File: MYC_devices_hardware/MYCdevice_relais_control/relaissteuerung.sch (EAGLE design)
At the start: 54 parts, among them IC1 MEGA8-P, IC2 7805T, K1 RT424012, K2 RT424012, K3 RT424012, K4 RT424012, Q1 20MHz, T1 BC547, T2 BC547, T3 BC547, T4 BC547

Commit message: adation to "0" based, and minor changes
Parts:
- removed C8: 18pF, resistor:C-EU050-025X075
- removed C9: 100nF, resistor:C-EU050-025X075
- removed R10: 3.3k, eagle-ltspice:R0204/7
- added JP2: ISP, jumper:JP3Q
- added R12: 3.3k, rcl:R-EU_0204/2V
- added X4, X5: 1503_09, con-lumberg:1503_09
- C1: value 100nF -> 22u 1206; device resistor:C-EU050-025X075 -> resistor:C-EUC1206
- C2, C3: value 47uF -> 22u 1206; device rcl:CPOL-EUTT5D10 -> resistor:C-EUC1206
- C4: value 100nF -> 18pF
- C6: device resistor:C-EU050-025X075 -> resistor:C-EUC1206
- D1, D2, D3, D4, D5: device diode:1N4004 -> zetex:D_E2L
- IC2: value 7805T -> 7805TV; device linear:7805T -> linear:7805TV
- R1, R2, R4, R6: device rcl:R-EU_0204/7 -> rcl:R-EU_0204/2V
- R8: device eagle-ltspice:R0204/7 -> rcl:R-EU_0204/2V
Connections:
- net N$37 renamed C5
- removed net N$1: IC1.PC4(ADC4/SDA), R2.2, SL1.5
- new net N$37: IC1.PC4(ADC4/SDA), R2.2, SL1.5, X4.3, X5.3
- new net N$56: C16.2, IC1.PB5(SCK), JP2.3, X1.-5
- net GND: now also C2.2, C3.1, C4.1, JP2.6, X4.1, X5.1; no longer C2.-, C3.-, C4.2, C8.1, C9.1
- net N$13: now also R8.2; no longer R6.1
- net N$15: now also R12.1; no longer R4.1
- net N$19: now also C4.2; no longer C8.2
- net N$22: now also R8.1; no longer R6.2
- net N$23: now also JP2.4
- net N$26: now also R6.1; no longer R8.1
- net N$3: no longer C2.+
- net N$33: now also JP2.1
- net N$34: now also R6.2; no longer R8.2
- net N$35: now also C3.2; no longer C9.2
- net N$36: now also R12.2; no longer R4.2
- net N$5: now also X4.2, X5.2
- net N$67: now also R4.2; no longer R10.2
- net N$69: now also R4.1; no longer R10.1
- net N$7: now also IC1.PC6(/RESET), JP2.5; no longer C16.2, IC1.PB5(SCK), X1.-5
- net VDD: now also C2.1, JP2.2; no longer C3.+, C4.1
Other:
- moved on the sheet: C1, C4, R4, R6, R8, SL1

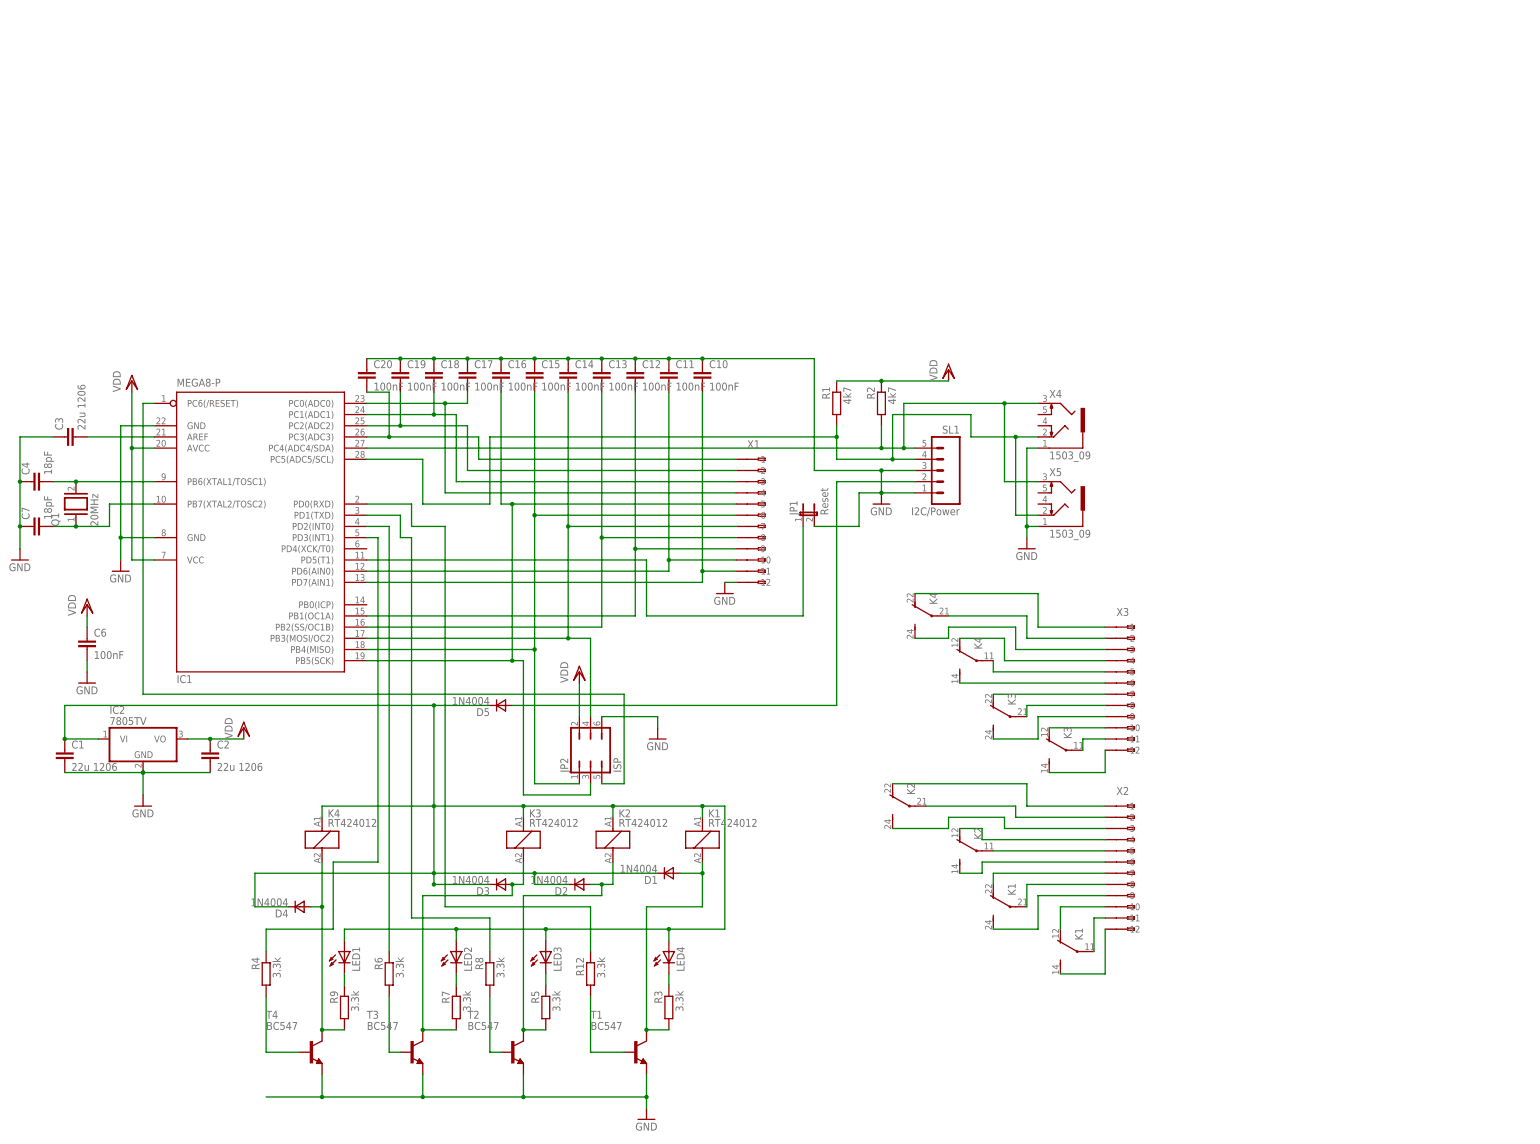
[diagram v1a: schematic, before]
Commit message: Modified Answer format
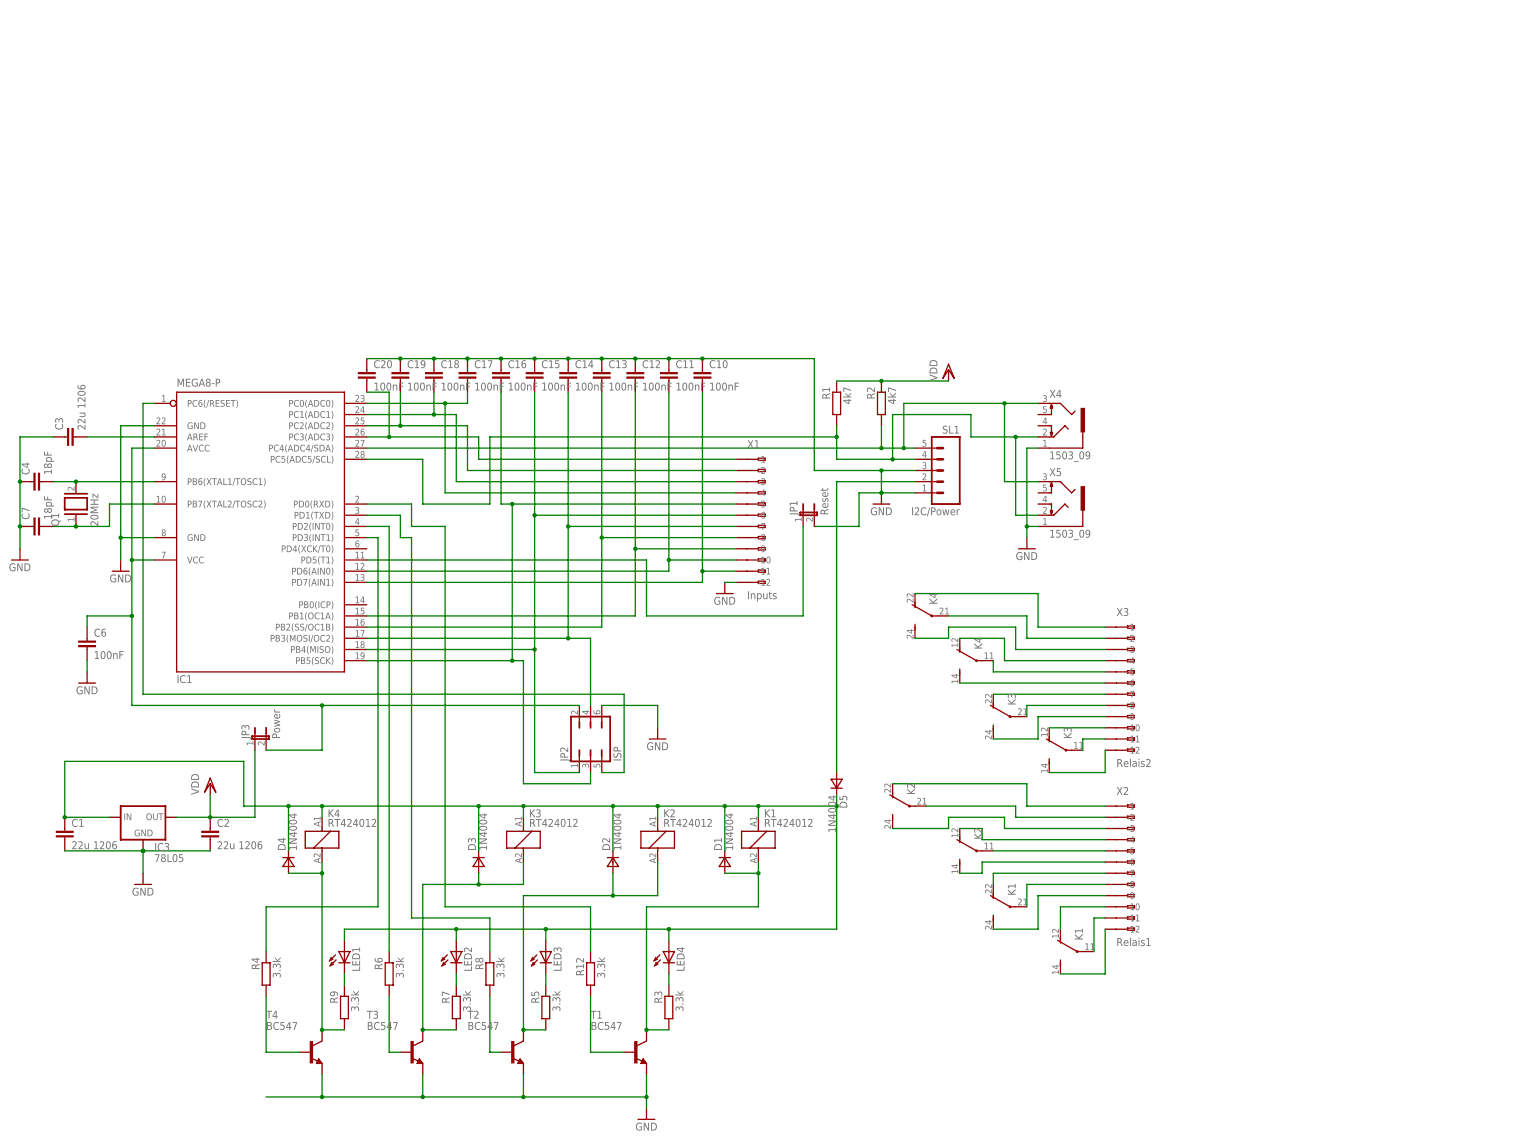
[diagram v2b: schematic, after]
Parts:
- removed IC2: 7805TV, linear:7805TV
- added IC3: 78L05, v-reg:78LXX
- added JP3: Power, jumper:JP1E
- R1, R2: device rcl:R-EU_0204/2V -> resistor:R-EU_R1206
- X1: value (none) -> Inputs
- X2: value (none) -> Relais1
- X3: value (none) -> Relais2
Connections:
- new net N$58: C6.1, IC1.AVCC, IC1.VCC@1, JP2.2, JP3.2
- net GND: now also IC3.GND; no longer IC2.GND
- net N$3: now also IC3.IN; no longer IC2.VI
- net VDD: now also IC3.OUT, JP3.1; no longer C6.1, IC1.AVCC, IC1.VCC@1, IC2.VO, JP2.2
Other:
- moved on the sheet: C1, C2, D1, D2, D3, D4, D5, JP2, K1, K2

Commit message: new connector, I2C with 3V
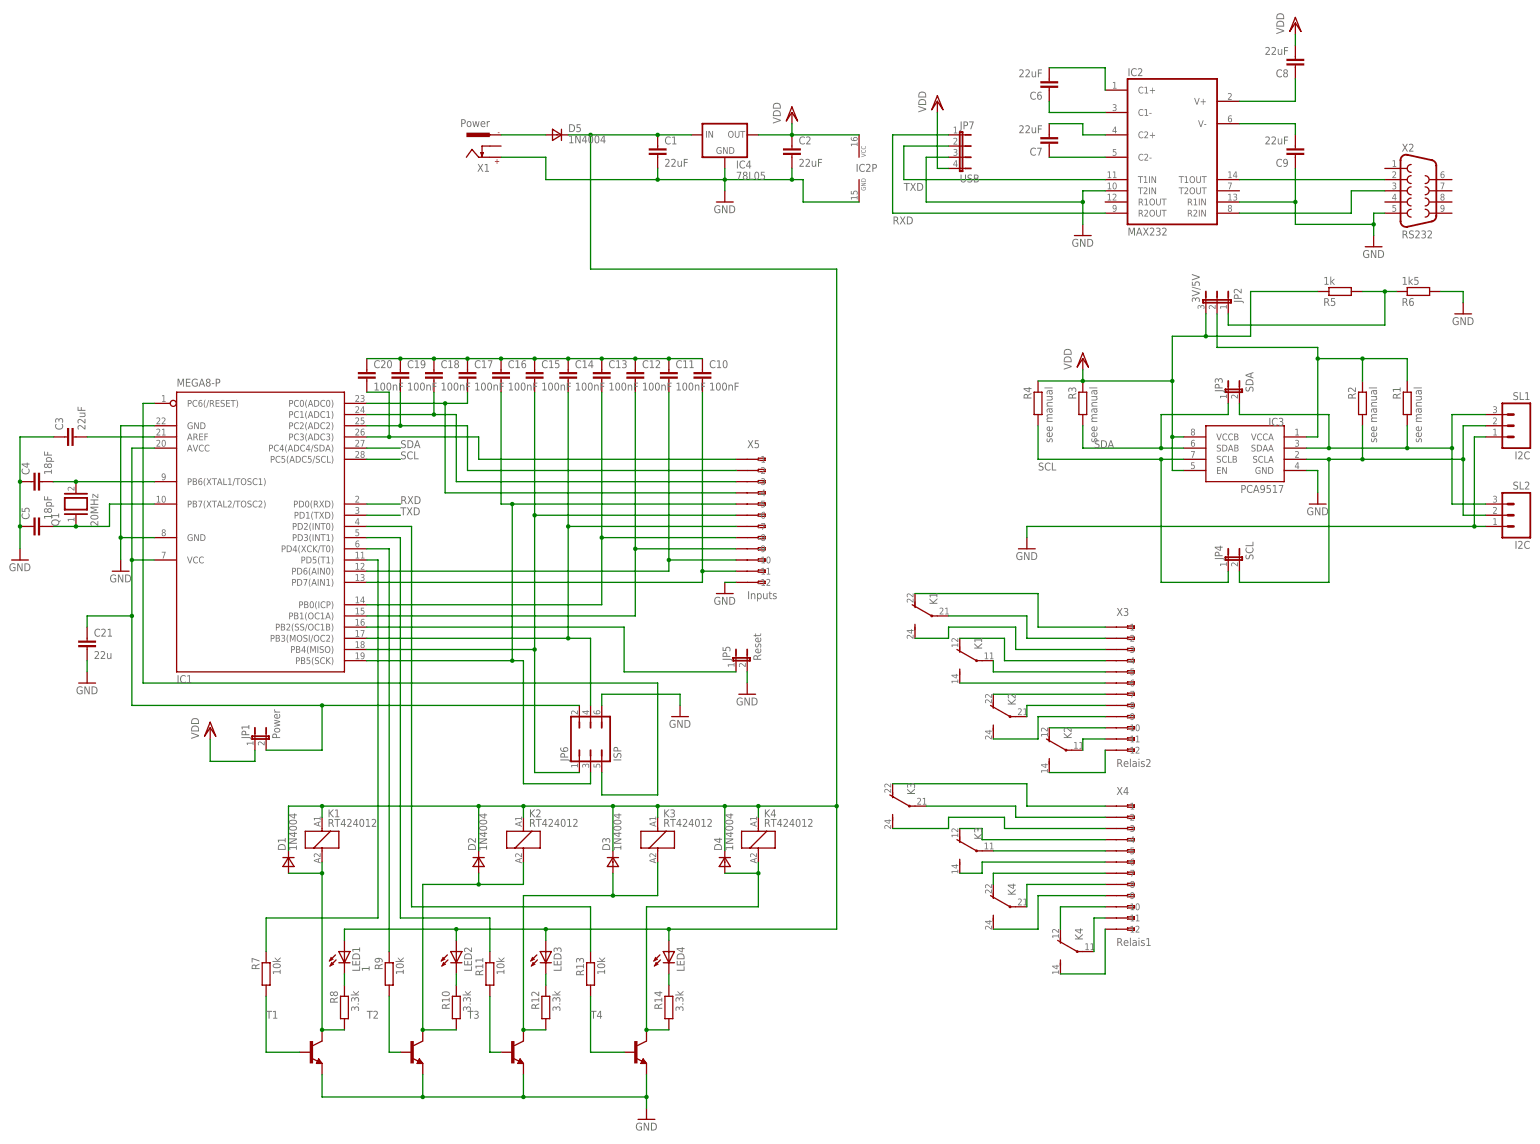
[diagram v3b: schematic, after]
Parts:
- added C21: 22u, resistor:C-EUC1206
- added C5: 18pF, resistor:C-EU050-025X075
- added C8, C9: 22uF, rcl:C-EUC1206
- added IC2: MAX232, maxim:MAX232
- added IC4: 78L05, v-reg:78LXX
- added JP4: SCL, jumper:JP1E
- added JP5: Reset, jumper:JP1E
- added JP6: ISP, jumper:JP3Q
- added JP7: USB, jumper:JP4E
- added R10, R14: 3.3k, rcl:R-EU_R1206
- added R11: 10k, rcl:R-EU_R1206
- added R13: 10k, rcl:R-EU_M1206
- added SL2: I2C, con-amp-quick:M03
- C1, C2, C3: value 22u 1206 -> 22uF
- C10, C11, C12, C13, C14, C15, C16, C17, C18, C19, C20: device resistor:C-EU050-025X075 -> resistor:C-EUC1206
- C6: value 100nF -> 22uF; device resistor:C-EUC1206 -> rcl:C-EUC1206
- C7: value 18pF -> 22uF; device resistor:C-EU050-025X075 -> rcl:C-EUC1206
- IC3: value 78L05 -> PCA9517; device v-reg:78LXX -> PCA9517:PCA9517
- JP1: value Reset -> Power
- JP2: value ISP -> 3V/5V; device jumper:JP3Q -> jumper:JP2E
- JP3: value Power -> SDA
- LED1: value (none) -> 1
- R1, R2: value 4k7 -> see manual
- R12, R8: device rcl:R-EU_0204/2V -> rcl:R-EU_R1206
- R3, R4: value 3.3k -> see manual; device rcl:R-EU_0204/2V -> resistor:R-EU_R1206
- R5: value 3.3k -> 1k; device rcl:R-EU_0204/2V -> resistor:R-EU_R1206
- R6: value 3.3k -> 1k5; device rcl:R-EU_0204/2V -> resistor:R-EU_R1206
- R7: value 3.3k -> 10k; device rcl:R-EU_0204/2V -> rcl:R-EU_R1206
- R9: value 3.3k -> 10k; device rcl:R-EU_0204/2V -> rcl:R-EU_M1206
- SL1: value I2C/Power -> I2C; device con-amp-quick:M05 -> con-amp-quick:M03
- T1, T2, T3, T4: value BC547 -> (none); device transistor:BC547 -> transistor-neu-to92:BC817-16-NPN-SOT23-BEC
- X1: value Inputs -> Power; device con-wago255:233-512 -> con-conrad:737992-55
- X2: value Relais1 -> RS232; device con-wago255:233-512 -> con-subd:F09H
- X4: value 1503_09 -> Relais1; device con-lumberg:1503_09 -> con-wago255:233-512
- X5: value 1503_09 -> Inputs; device con-lumberg:1503_09 -> con-wago255:233-512
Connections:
- new net N$57: IC3.SDAA, JP3.2, R1.2, SL1.3, SL2.3
- new net N$59: IC3.VCCA, JP2.2, R1.1, R2.1
- new net N$60: IC2G$1.T1OUT, X2.2
- new net N$63: JP2.1, R5.2, R6.1
- new net N$64: IC2G$1.R2IN, X2.3
- new net N$70: C9.2, IC2G$1.V-
- new net N$71: C8.1, IC2G$1.V+
- new net N$72: C7.1, IC2G$1.C2-
- new net N$73: C7.2, IC2G$1.C2+
- new net N$74: C6.1, IC2G$1.C1-
- new net N$75: C6.2, IC2G$1.C1+
- new net RXD: IC1.PD0(RXD), IC2G$1.R2OUT, JP7.1
- new net SCL: IC1.PC5(ADC5/SCL), IC3.SCLB, JP4.1, R4.2
- new net SDA: IC1.PC4(ADC4/SDA), IC3.SDAB, JP3.1, R3.2
- new net TXD: IC1.PD1(TXD), IC2G$1.T1IN, JP7.2
- net C5: now also C5.2; no longer C7.2
- net GND: now also C21.2, C5.1, C9.1, IC2G$1.R1IN, IC2G$1.T2IN, IC2P.GND, IC4.GND, JP5.2, JP6.6, JP7.3, R6.2, SL2.1, X1.+, X2.5, X5.-12; no longer C10.1, C11.1, C12.1, C13.1, C14.1, C15.1, C16.1, C17.1, C18.1, C19.1, C20.1, C6.2, C7.1, JP1.2, JP2.6, SL1.3, X1.-12, X4.1, X5.1
- net N$10: now also K43.S, X4.-9; no longer K13.S, X2.-9
- net N$11: now also K43.P, X4.-8; no longer K13.P, X2.-8
- net N$12: now also K43.O, X4.-7; no longer K13.O, X2.-7
- net N$13: now also R11.2, T3.B; no longer R8.2, T2.B
- net N$15: now also IC1.PD5(T1), R7.1; no longer IC1.PD0(RXD), R12.1
- net N$16: now also K32.S, X4.-6; no longer K22.S, X2.-6
- net N$17: now also K32.P, X4.-5; no longer K22.P, X2.-5
- net N$18: now also K32.O, X4.-4; no longer K22.O, X2.-4
- net N$2: now also K42.S, X4.-12; no longer K12.S, X2.-12
- net N$20: now also X5.-3; no longer X1.-3
- net N$21: now also IC1.PB2(SS/OC1B), JP5.1; no longer IC1.PD5(T1), JP1.1
- net N$22: now also IC1.PD4(XCK/T0), R9.1; no longer IC1.PD1(TXD), R8.1
- net N$23: now also JP6.4, X5.-7; no longer JP2.4, X1.-7
- net N$24: now also IC1.PB0(ICP), X5.-8; no longer IC1.PB2(SS/OC1B), X1.-8
- net N$25: now also X1.-1; no longer SL1.2
- net N$26: now also R13.1; no longer R6.1
- net N$27: now also K33.S, X4.-3; no longer K23.S, X2.-3
- net N$28: now also K33.P, X4.-2; no longer K23.P, X2.-2
- net N$29: now also R14.1; no longer R3.1
- net N$3: now also IC4.IN; no longer IC3.IN
- net N$30: now also R12.1; no longer R5.1
- net N$31: now also X5.-9; no longer X1.-9
- net N$32: now also R10.1; no longer R7.1
- net N$33: now also JP6.1, X5.-6; no longer JP2.1, X1.-6
- net N$34: now also R9.2, T2.B; no longer R6.2, T3.B
- net N$36: now also R13.2, T4.B; no longer R12.2, T1.B
- net N$37: now also IC3.SCLA, JP4.2, SL1.2, SL2.2; no longer IC1.PC4(ADC4/SDA), SL1.5, X4.3, X5.3
- net N$38: now also X5.-2; no longer X1.-2
- net N$39: now also K33.O, X4.-1; no longer K23.O, X2.-1
- net N$4: now also X5.-1; no longer X1.-1
- net N$40: now also D2.A, K21.2, R10.2, T2.C; no longer D3.A, K31.2, R7.2, T3.C
- net N$41: now also D3.A, K31.2, R12.2, T3.C; no longer D2.A, K21.2, R5.2, T2.C
- net N$42: now also D4.A, K41.2, R14.2, T4.C; no longer D1.A, K11.2, R3.2, T1.C
- net N$43: now also K22.S; no longer K32.S
- net N$44: now also K22.P; no longer K32.P
- net N$45: now also K22.O; no longer K32.O
- net N$46: now also K23.P; no longer K33.P
- net N$47: now also K23.S; no longer K33.S
- net N$48: now also K23.O; no longer K33.O
- net N$49: now also K12.S; no longer K42.S
- net N$5: now also C10.1, C11.1, C12.1, C13.1, C14.1, C15.1, C16.1, C17.1, C18.1, C19.1, C20.1; no longer IC1.PC5(ADC5/SCL), R1.2, SL1.4, X4.2, X5.2
- net N$50: now also K12.P; no longer K42.P
- net N$51: now also K12.O; no longer K42.O
- net N$52: now also K13.S; no longer K43.S
- net N$53: now also K13.P; no longer K43.P
- net N$54: now also K13.O; no longer K43.O
- net N$55: now also X5.-10; no longer X1.-10
- net N$56: now also JP6.3, X5.-5; no longer JP2.3, X1.-5
- net N$58: now also C21.1, JP1.2, JP6.2; no longer C6.1, JP2.2, JP3.2
- net N$6: now also K42.P, X4.-11; no longer K12.P, X2.-11
- net N$62: now also X5.-11; no longer X1.-11
- net N$65: now also R8.1; no longer R9.1
- net N$66: now also D1.A, K11.2, R8.2, T1.C; no longer D4.A, K41.2, R9.2, T4.C
- net N$67: now also R7.2, T1.B; no longer R4.2, T4.B
- net N$69: now also R11.1; no longer R4.1
- net N$7: now also JP6.5; no longer JP2.5
- net N$8: now also X5.-4; no longer X1.-4
- net N$9: now also K42.O, X4.-10; no longer K12.O, X2.-10
- net VDD: now also C8.2, IC2P.VCC, IC3.EN, IC3.VCCB, IC4.OUT, JP1.1, JP2.3, JP7.4, R3.1, R4.1, R5.1; no longer IC3.OUT, JP3.1, R1.1, R2.1
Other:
- moved on the sheet: C1, C2, C6, C7, D1, D2, D3, D4, D5, JP1, JP3, K1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
